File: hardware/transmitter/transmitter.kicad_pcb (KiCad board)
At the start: 2 copper layers, 85.1 x 63.5 mm, 23 parts, among them J1 Screw_Terminal_01x05, P5 Digital, P6 Analog, U1 uA7805, U2 TMP36, U3 JSN-SR04T-2.0, U4 MAX3232

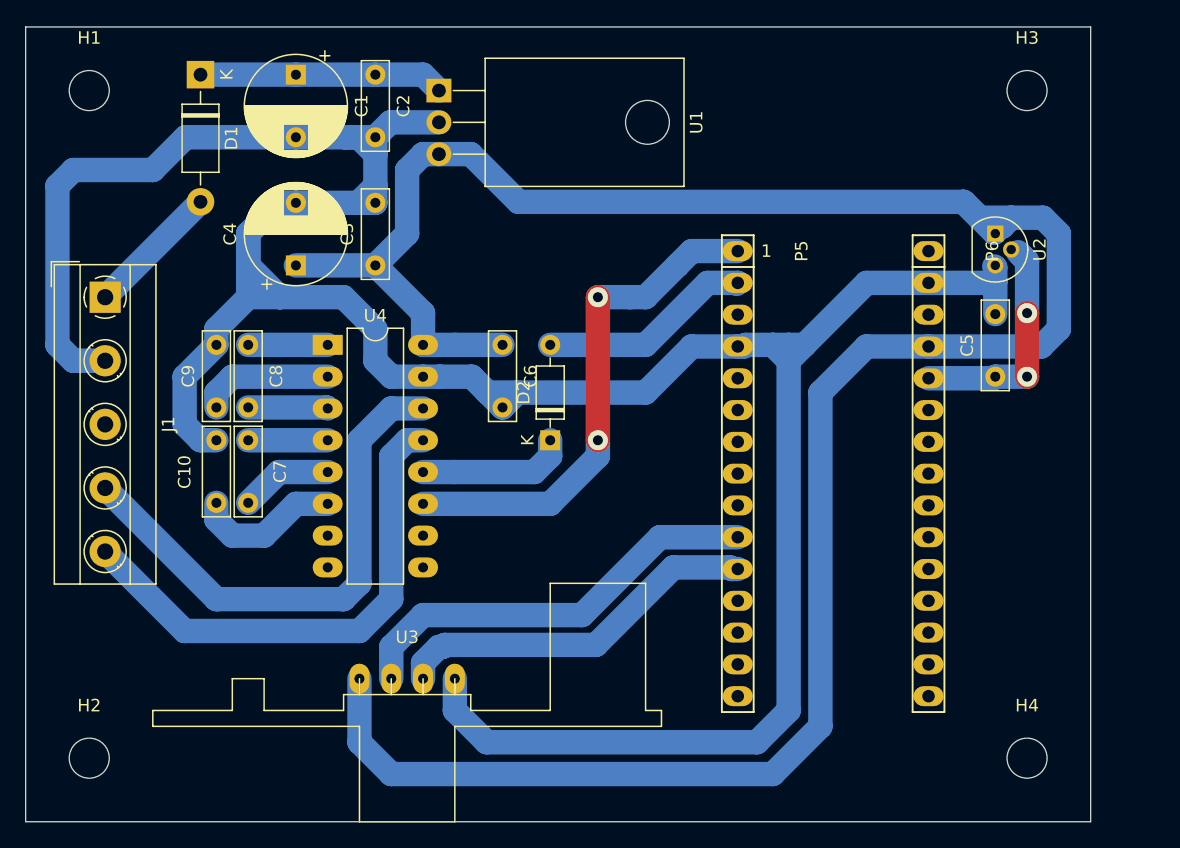
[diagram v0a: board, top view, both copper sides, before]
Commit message: added copper zone
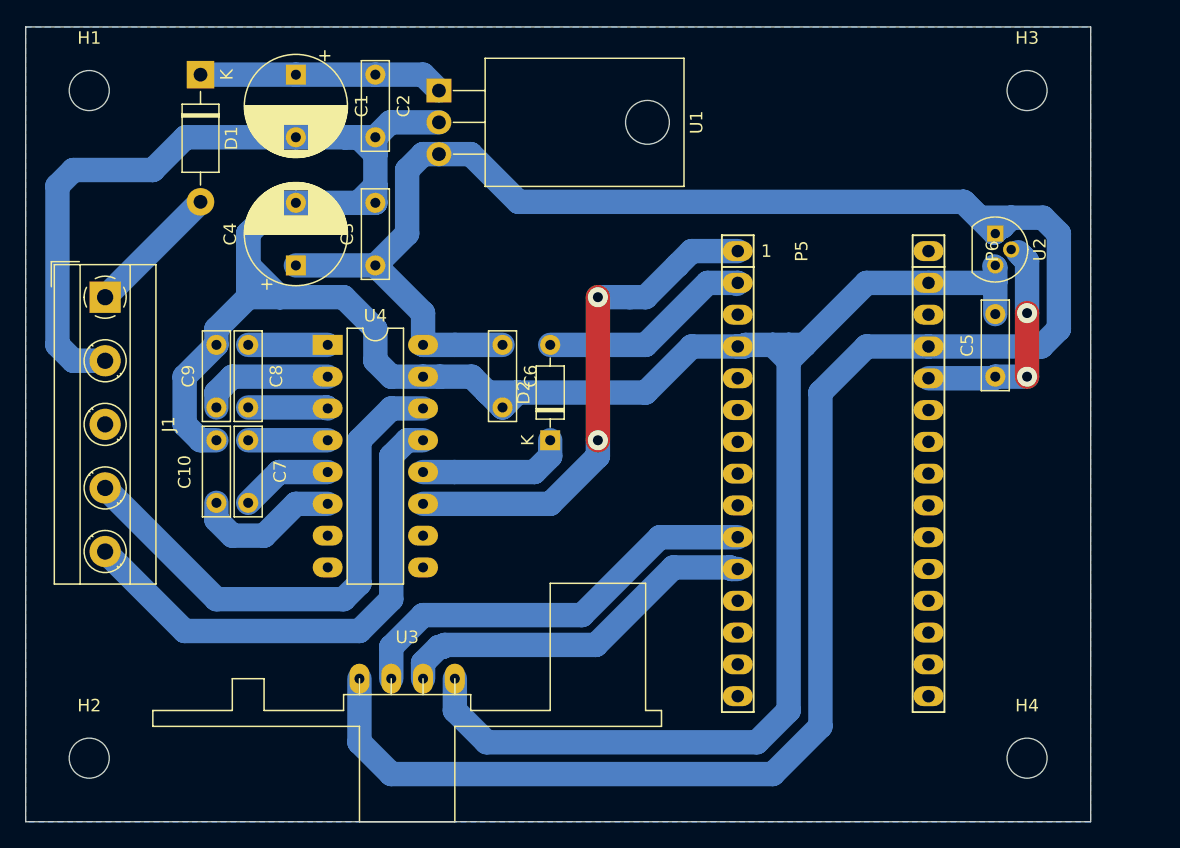
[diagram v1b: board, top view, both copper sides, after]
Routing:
- added copper zone on B.Cu, net GND
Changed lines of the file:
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@@
   (segment (start 69.85 87.63) (end 78.74 96.52) (width 1.95) (layer B.Cu) (net 38))
   (segment (start 78.74 96.52) (end 88.9 96.52) (width 1.95) (layer B.Cu) (net 38))
+  (zone (net 4) (net_name GND) (layer B.Cu) (hatch edge 0.508)
+    (connect_pads (clearance 0.508))
+    (min_thickness 0.254)
+    (fill yes (arc_segments 32) (thermal_gap 0.508) (thermal_bridge_width 0.508))
+    (polygon
+      (pts
+        (xy 63.5 50.8) (xy 148.59 50.8) (xy 148.59 114.3) (xy 63.5 114.3)
+      )
+    )
+  )
 )

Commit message: copper zone reviewed (clearance, minimum with, solid pad connection)
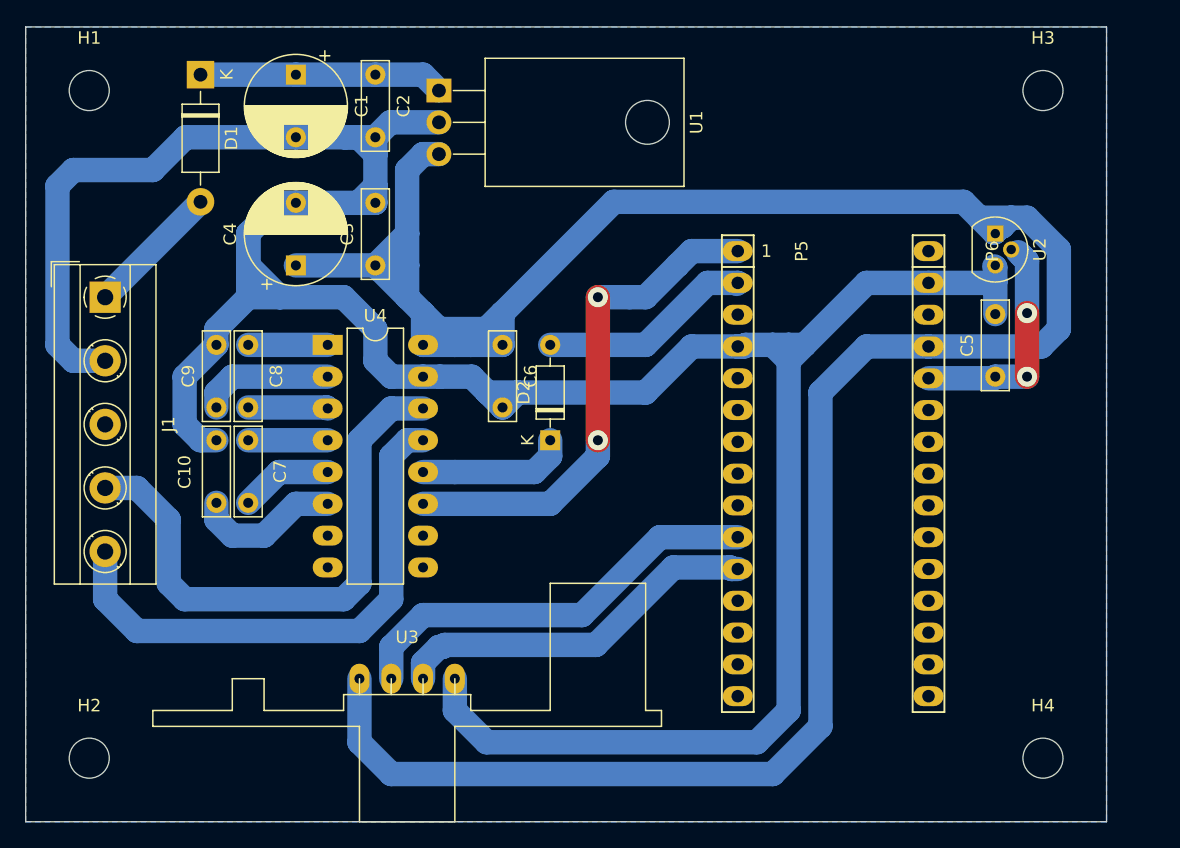
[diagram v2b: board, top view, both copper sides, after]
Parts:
- moved H3 1.27 mm to (144.8, 55.9)
- moved H4 1.27 mm to (144.8, 109.2)
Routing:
- net +5V: track 189.9 -> 207.4 mm
- net /TXD_connector: track 42.1 -> 45.1 mm
- net /RXD_connector: track 41.0 -> 43.3 mm
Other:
- board size 85.1 x 63.5 mm -> 86.4 x 63.5 mm

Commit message: pcb narrowed by 5 mm
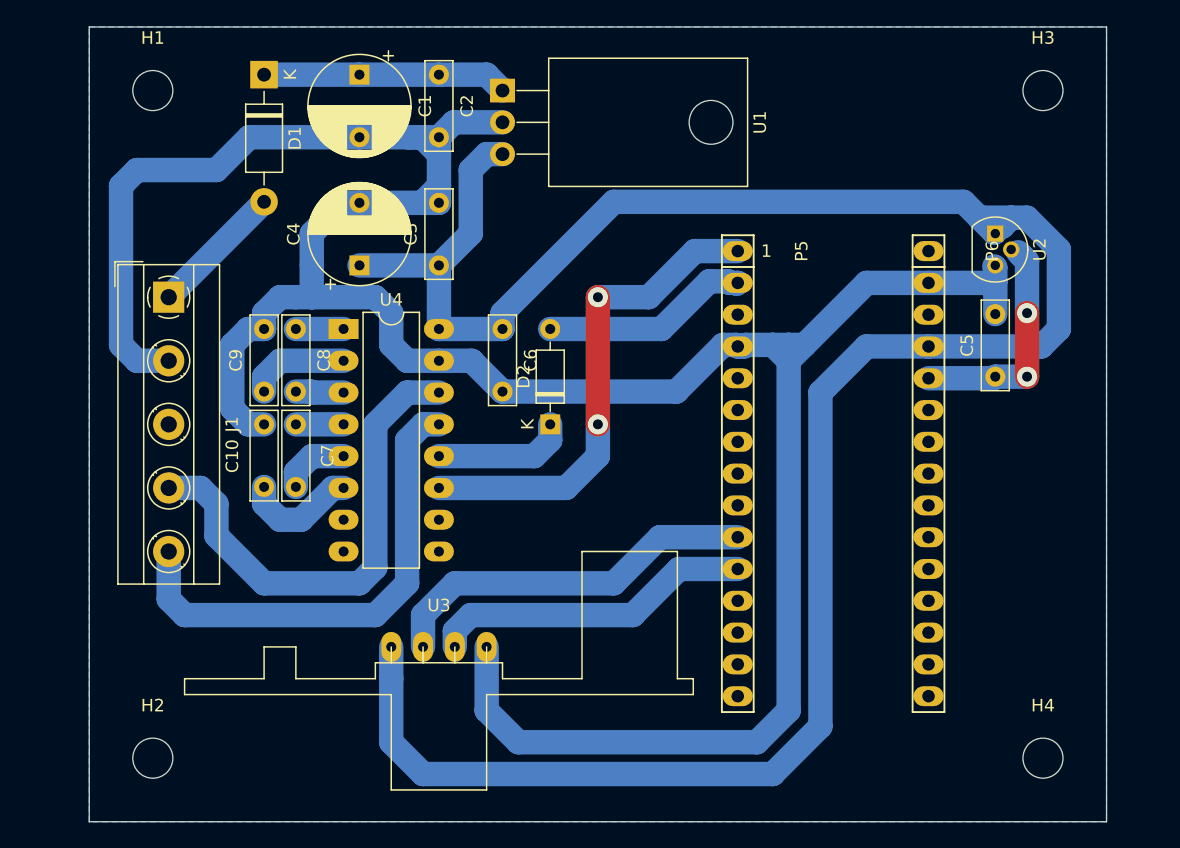
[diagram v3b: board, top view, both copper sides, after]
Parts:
- moved J1 5.08 mm to (74.9, 72.4)
- moved C1 5.08 mm to (90.2, 54.6)
- moved C2 5.08 mm to (96.5, 54.6)
- moved C3 5.08 mm to (96.5, 69.8)
- moved C4 5.08 mm to (90.2, 69.8)
- moved D1 5.08 mm to (82.5, 54.6)
- moved H1 5.08 mm to (73.7, 55.9)
- moved H2 5.08 mm to (73.7, 109.2)
- moved U1 5.08 mm to (101.6, 55.9)
- moved C10 4.02 mm to (82.5, 87.5)
- moved C7 4.02 mm to (85.1, 82.5)
- moved C8 4.02 mm to (85.1, 74.9)
- moved C9 4.02 mm to (82.5, 79.9)
- moved U3 3.59 mm to (96.5, 96.5)
- moved U4 1.80 mm to (88.9, 74.9)
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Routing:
- net +5V: track 207.4 -> 181.6 mm
- net GND: track 236.9 -> 223.8 mm
- net /TXD_connector: track 45.1 -> 39.2 mm
- net /RXD_connector: track 43.3 -> 38.9 mm
- net /8: track 29.6 -> 25.9 mm
- net /7: track 33.9 -> 30.3 mm
- net Net-(C8-Pad2): track 6.38 -> 3.84 mm
- net Net-(C8-Pad1): track 6.35 -> 3.81 mm
- net Net-(C7-Pad1): track 6.35 -> 3.81 mm
- net Net-(C9-Pad1): track 10.6 -> 8.07 mm
- net Net-(C10-Pad1): track 11.8 -> 9.28 mm
- net Net-(C7-Pad2): track 7.37 -> 5.53 mm
- net /1(Tx): track 40.9 -> 39.2 mm
- net Net-(D2-Pad1): track 12.0 -> 10.7 mm
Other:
- board size 86.4 x 63.5 mm -> 81.3 x 63.5 mm

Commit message: resized board to 85,090 mm x 53,340 mm
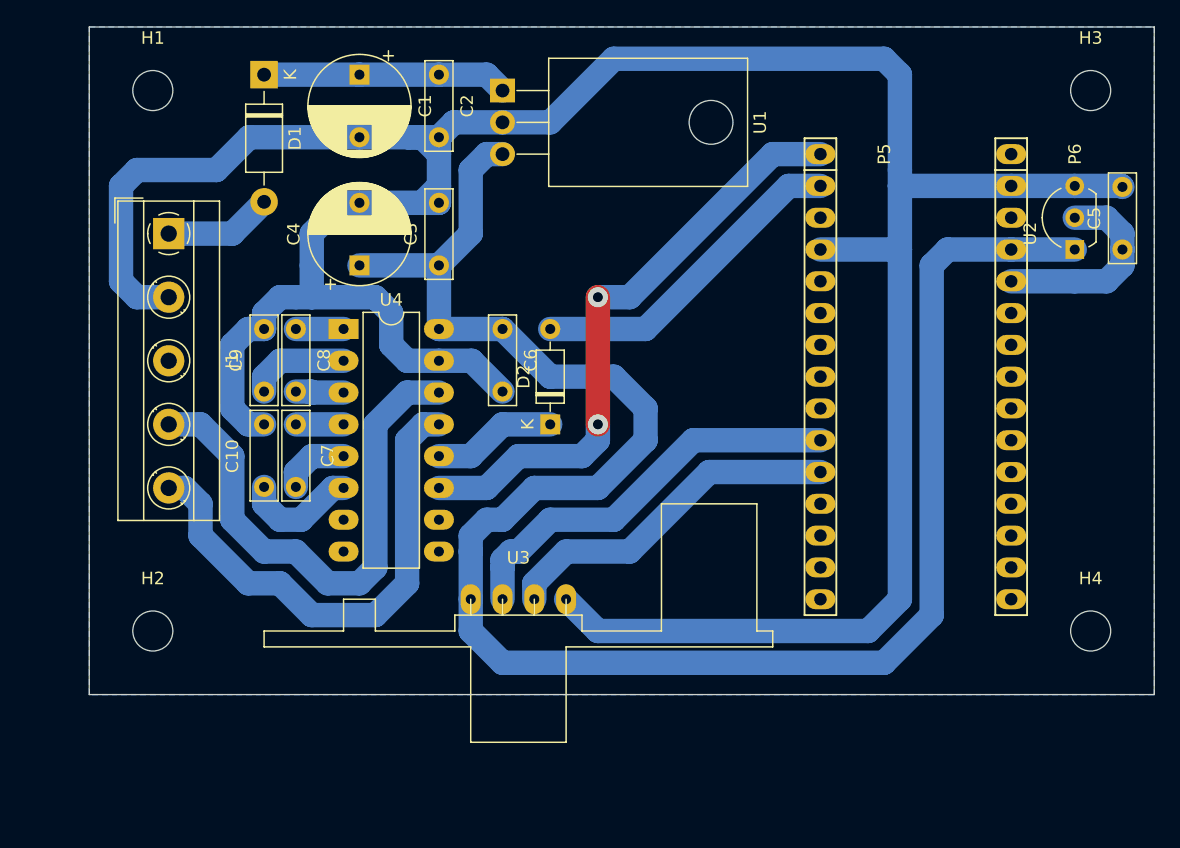
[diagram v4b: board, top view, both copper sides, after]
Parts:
- U2: footprint Package_TO_SOT_THT:TO-92 -> Package_TO_SOT_THT:TO-92L_Inline_Wide
- moved C5 14.4 mm to (151.1, 68.6)
- moved H4 10.9 mm to (148.6, 99.1)
- moved P6 10.2 mm to (142.2, 61.0)
- moved P5 10.2 mm to (127.0, 61.0)
- moved H2 10.2 mm to (73.7, 99.1)
- moved U3 7.41 mm to (102.9, 92.7)
- moved U2 6.48 mm to (147.3, 68.6), turned to 90 degrees
- moved J1 5.08 mm to (74.9, 67.3)
- moved H3 3.81 mm to (148.6, 55.9)
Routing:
- net +5V: track 181.6 -> 149.0 mm
- net GND: track 223.8 -> 236.9 mm
- net /0(Rx): track 16.7 -> 26.3 mm
- net /1(Tx): track 39.2 -> 48.2 mm
- net /TXD_connector: track 39.2 -> 42.8 mm
- net /7: track 30.3 -> 32.5 mm
- net /Vin_connector: track 10.8 -> 8.67 mm
- net /8: track 25.9 -> 27.8 mm
- net /A7: track 18.2 -> 16.3 mm, vias 2 -> 0
- net /RXD_connector: track 38.9 -> 40.3 mm
- net Net-(D2-Pad1): track 10.7 -> 9.94 mm
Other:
- board size 81.3 x 63.5 mm -> 85.1 x 53.3 mm
- board text removed: "1"
